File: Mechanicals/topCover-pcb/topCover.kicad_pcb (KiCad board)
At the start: 2 copper layers, 89 x 100 mm, 1 part

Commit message: updated documentation + wrote test script
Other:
- board text removed: "JLCJLCJLCJLC"
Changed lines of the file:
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@@
-(kicad_pcb (version 20171130) (host pcbnew "(5.1.2)-1")
+(kicad_pcb (version 20171130) (host pcbnew 5.1.5-52549c5~84~ubuntu19.10.1)
   (general
     (thickness 1.6)
-    (drawings 1)
+    (drawings 0)
     (tracks 0)
     (zones 0)
@@
     (fp_arc (start -36.83 1.27) (end -37.03 1.270001) (angle -90) (layer Edge.Cuts) (width 0.2))
   )
-  (gr_text JLCJLCJLCJLC (at 141.7 83.7) (layer B.SilkS)
-    (effects (font (size 1.5 1.5) (thickness 0.2)) (justify mirror))
-  )
 )

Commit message: update board
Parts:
- removed the REF** at (143.9, 98.6)
- added REF**: MountingHole_3.2mm_M3, MountingHole:MountingHole_3.2mm_M3, F.Cu at (188.2, 148.6)
- added REF**: MountingHole_3.2mm_M3, MountingHole:MountingHole_3.2mm_M3, F.Cu at (105.2, 148.6)
- added REF**: MountingHole_3.2mm_M3, MountingHole:MountingHole_3.2mm_M3, F.Cu at (105.2, 54.5)
- added REF**: MountingHole_3.2mm_M3, MountingHole:MountingHole_3.2mm_M3, F.Cu at (188.2, 54.5)
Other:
- outline, holes or cut-outs redrawn

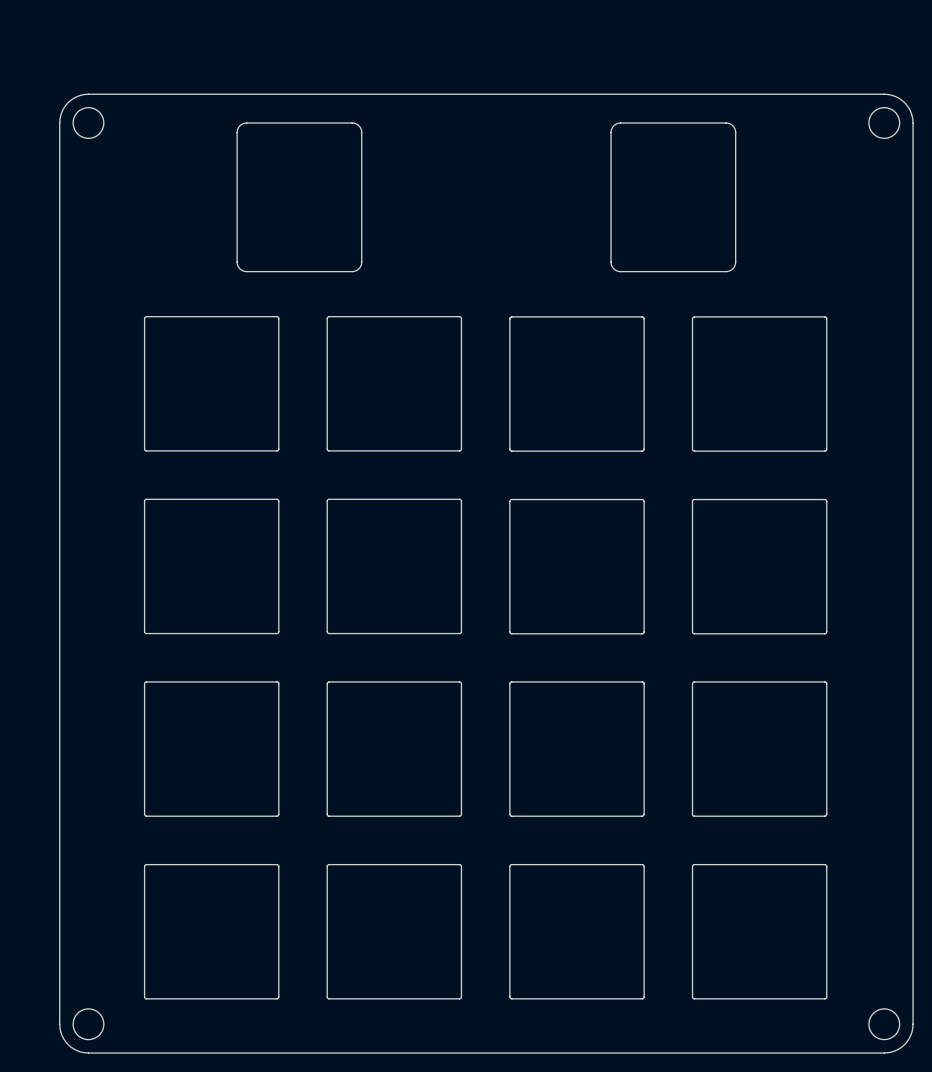
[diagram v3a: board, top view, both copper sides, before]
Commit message: move res with HS interference
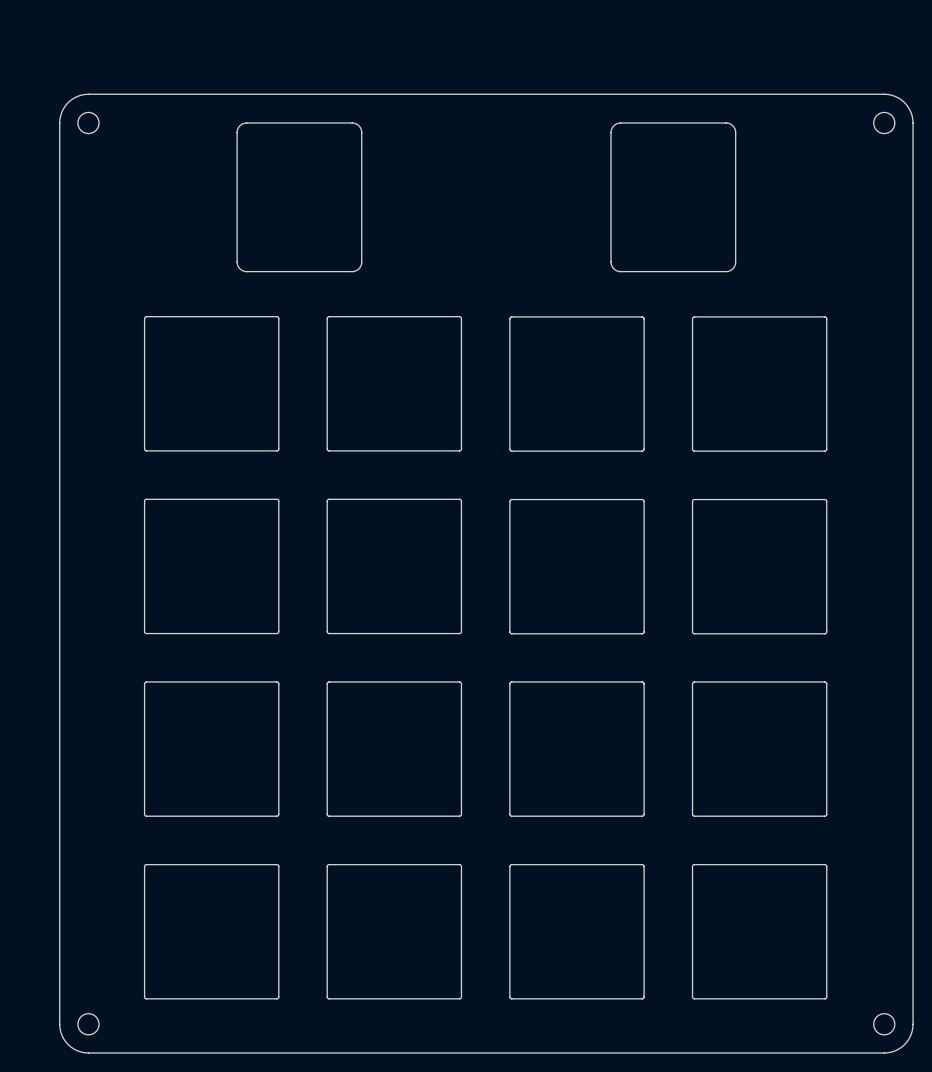
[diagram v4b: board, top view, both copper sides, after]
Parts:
- REF** (x4): value MountingHole_3.2mm_M3 -> MountingHole_2.2mm_M2; footprint MountingHole:MountingHole_3.2mm_M3 -> MountingHole:MountingHole_2.2mm_M2
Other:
- outline, holes or cut-outs redrawn
